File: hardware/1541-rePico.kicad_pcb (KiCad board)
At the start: 2 copper layers, 59.1 x 60 mm, 23 parts, among them IC2 VIA6522, J1 Conn_01x01_Pin, J2 RESET_1541, J3 SD Card Module Connector, J4 EXT_5V, J5 Display Power, J6 Conn_01x05_Pin, J7 Display Connector, P1 VIA_PIN_1-20, P2 VIA_PIN_21-40, SW1 RESET, U1 Pico, U2 TXS0108EPW, U3 TXS0108EPW

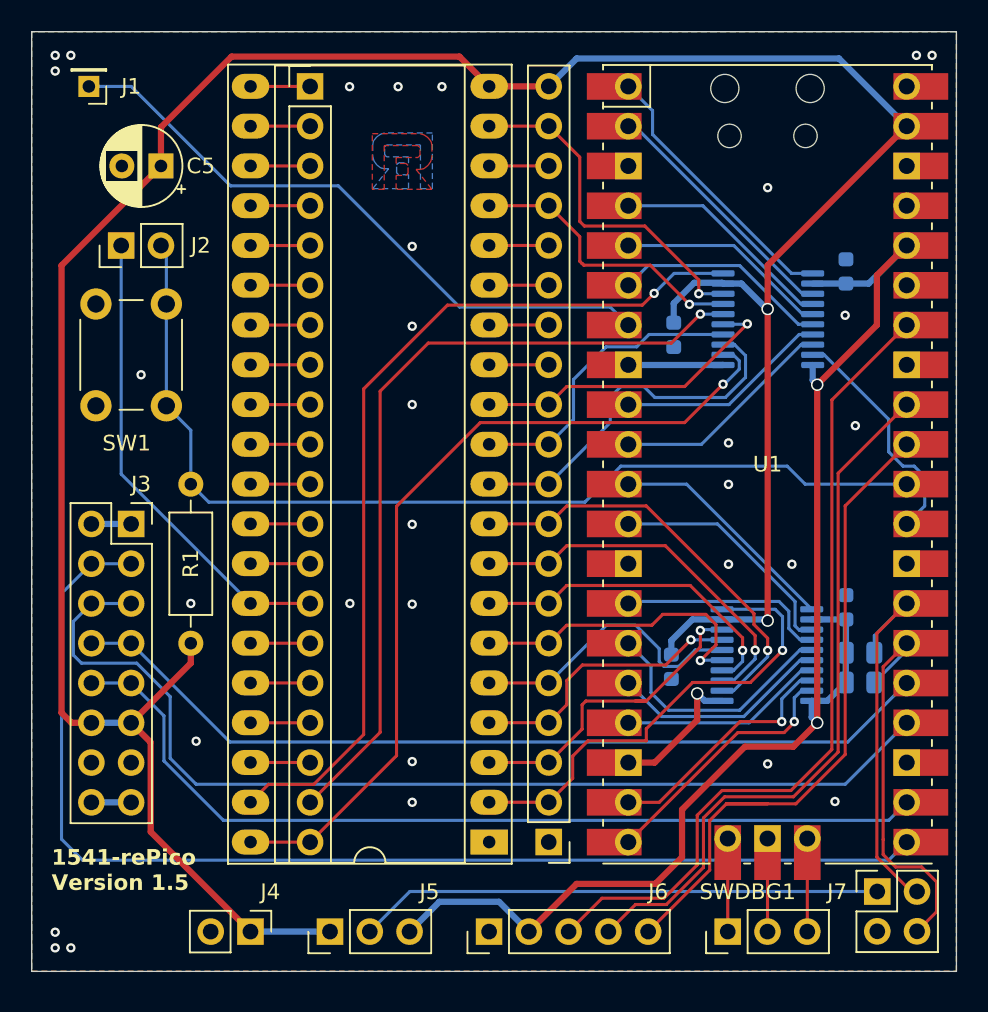
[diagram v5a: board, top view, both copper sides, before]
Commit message: PCB version 1.6
- use of SN74LVC4245A for levelshifting of PortB-Signals
-> needed an inverted Mode/OE signal for DIR (done via BSS138)
- use of BSS138 for shifting of basic signals (MTR, STP,...)
- cut off "mode/OE" pin from Gatearray -> tied to GND to not let it drive PortB
- rerouted the PCB again -> alignment of Pinheaders and vias
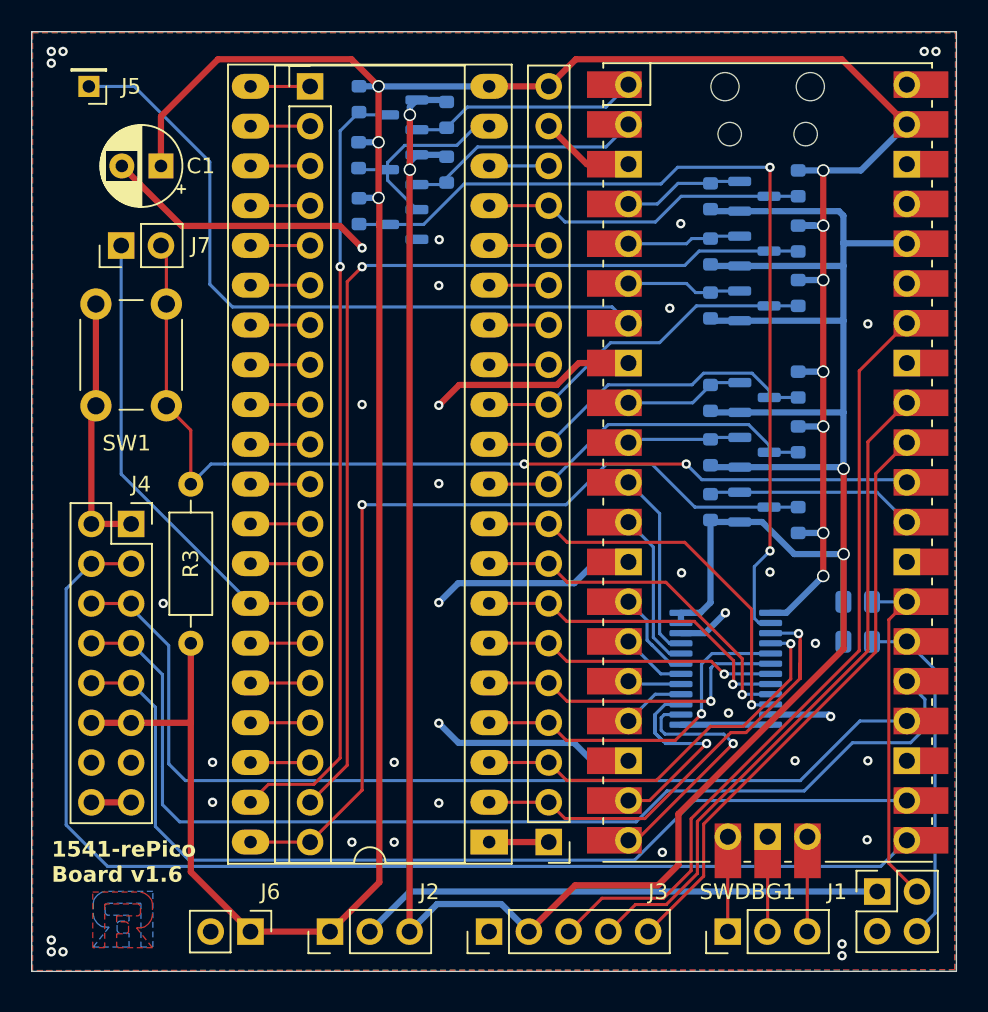
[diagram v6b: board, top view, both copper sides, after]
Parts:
- removed the C1 at (141.2, 84.4)
- removed C2, C3, C4: 0,1µF, Capacitor_SMD:C_0603_1608Metric
- removed U3: TXS0108EPW, Package_SO:TSSOP-20_4.4x6.5mm_P0.65mm
- added Q1: BSS138, Package_TO_SOT_SMD:SOT-23, B.Cu at (123.8, 77.4)
- added Q2: BSS138, Package_TO_SOT_SMD:SOT-23, B.Cu at (146.3, 91.9)
- added Q3: BSS138, Package_TO_SOT_SMD:SOT-23, B.Cu at (146.3, 88.4)
- added Q4: BSS138, Package_TO_SOT_SMD:SOT-23, B.Cu at (146.3, 82.6)
- added Q5: BSS138, Package_TO_SOT_SMD:SOT-23, B.Cu at (146.3, 75.6)
- added Q6: BSS138, Package_TO_SOT_SMD:SOT-23, B.Cu at (123.8, 73.9)
- added Q7: BSS138, Package_TO_SOT_SMD:SOT-23, B.Cu at (146.3, 95.4)
- added Q8: BSS138, Package_TO_SOT_SMD:SOT-23, B.Cu at (123.8, 70.4)
- added Q9: BSS138, Package_TO_SOT_SMD:SOT-23, B.Cu at (146.3, 79.1)
- added R10: 10k, Resistor_SMD:R_0603_1608Metric, B.Cu at (149.1, 81.7)
- added R11: 10k, Resistor_SMD:R_0603_1608Metric, B.Cu at (143.5, 75.6)
- added R12: 10k, Resistor_SMD:R_0603_1608Metric, B.Cu at (149.1, 74.7)
- added R13: 10k, Resistor_SMD:R_0603_1608Metric, B.Cu at (126.7, 73.9)
- added R14: 10k, Resistor_SMD:R_0603_1608Metric, B.Cu at (121.1, 72.9)
- added R15: 10k, Resistor_SMD:R_0603_1608Metric, B.Cu at (143.5, 95.4)
- added R16: 10k, Resistor_SMD:R_0603_1608Metric, B.Cu at (149.1, 96.2)
- added R17: 10k, Resistor_SMD:R_0603_1608Metric, B.Cu at (126.7, 70.4)
- added R18: 10k, Resistor_SMD:R_0603_1608Metric, B.Cu at (121.1, 69.4)
- added R19: 10k, Resistor_SMD:R_0603_1608Metric, B.Cu at (143.5, 79.1)
- added R20: 10k, Resistor_SMD:R_0603_1608Metric, B.Cu at (149.1, 78.3)
- added R4: 1M, Resistor_SMD:R_0603_1608Metric, B.Cu at (121.1, 76.5)
- added R5: 10k, Resistor_SMD:R_0603_1608Metric, B.Cu at (143.5, 91.9)
- added R6: 10k, Resistor_SMD:R_0603_1608Metric, B.Cu at (149.1, 91.1)
- added R7: 10k, Resistor_SMD:R_0603_1608Metric, B.Cu at (143.5, 88.4)
- added R8: 10k, Resistor_SMD:R_0603_1608Metric, B.Cu at (149.1, 87.6)
- added R9: 10k, Resistor_SMD:R_0603_1608Metric, B.Cu at (143.5, 82.5)
- U2: value TXS0108EPW -> SN74LVC4245A; footprint Package_SO:TSSOP-20_4.4x6.5mm_P0.65mm -> Package_SO:TSSOP-24_4.4x7.8mm_P0.65mm
- moved R1 3.25 mm to (152.9, 101.5)
- moved U2 2.77 mm to (144.5, 105.7)
- moved R2 2.60 mm to (152.9, 104.0)
- moved U1 0.12 mm to (147.2, 92.6)
- renumbered C5 to C1, IC2 to IC1, J7 to J1, J5 to J2, J6 to J3, J3 to J4, J1 to J5, J4 to J6, J2 to J7, R2 to R1, R3 to R2, R1 to R3
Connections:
- P1 pad 19: /VIA 6522 Sockel/MODE -> GND
- U2 pad 1: /_PA0 -> +5V
- U2 pad 10: +3.3V -> /VIA 6522 Sockel/PA7
- U2 pad 12: /VIA 6522 Sockel/PA7 -> GND
- U2 pad 13: /VIA 6522 Sockel/PA6 -> GND
- U2 pad 14: /VIA 6522 Sockel/PA5 -> /_PA7
- U2 pad 15: /VIA 6522 Sockel/PA4 -> /_PA6
- U2 pad 16: /VIA 6522 Sockel/PA3 -> /_PA5
- U2 pad 17: /VIA 6522 Sockel/PA2 -> /_PA4
- U2 pad 18: /VIA 6522 Sockel/PA1 -> /_PA3
- U2 pad 19: +5V -> /_PA2
- U2 pad 2: +3.3V -> Net-(Q1-D)
- U2 pad 20: /VIA 6522 Sockel/PA0 -> /_PA1
- U2 pad 3: /_PA1 -> /VIA 6522 Sockel/PA0
- U2 pad 4: /_PA2 -> /VIA 6522 Sockel/PA1
- U2 pad 5: /_PA3 -> /VIA 6522 Sockel/PA2
- U2 pad 6: /_PA4 -> /VIA 6522 Sockel/PA3
- U2 pad 7: /_PA5 -> /VIA 6522 Sockel/PA4
- U2 pad 8: /_PA6 -> /VIA 6522 Sockel/PA5
- U2 pad 9: /_PA7 -> /VIA 6522 Sockel/PA6
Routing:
- net +3.3V: track 86.6 -> 194.6 mm, vias 2 -> 4
- net GND: track 20.3 -> 99.2 mm, vias 32 -> 38
- net Net-(Q1-D): track 0.00 -> 58.1 mm, vias 0 -> 2
- net +5V: track 177.1 -> 193.6 mm, vias 2 -> 10
- net MOSI: track 56.2 -> 68.8 mm
- net /_PA3: track 16.1 -> 4.21 mm
- net /VIA 6522 Sockel/SOE_GA: track 52.0 -> 63.9 mm
- net /_PA4: track 14.1 -> 3.43 mm
- net /VIA 6522 Sockel/MODE: track 22.3 -> 13.1 mm, vias 1 -> 0
- net /_PA5: track 13.1 -> 4.06 mm
- net /_PA2: track 13.4 -> 5.82 mm
- net /_STP1: track 14.4 -> 7.25 mm
- net /VIA 6522 Sockel/SOE: track 57.5 -> 50.5 mm
- net /_MTR: track 13.9 -> 7.38 mm
- net /_SYNC: track 14.4 -> 8.07 mm
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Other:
- board text added: "1541-rePico Board v1.6"
- board text added: "https://github.com/fook42/1541-rePico"
- board text removed: "1541-rePico Version 1.5"
- board text removed: "https://github.com/fook42/1541-repico"

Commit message: updated PDFs for PCB v1.6
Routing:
- net GND: track 99.2 -> 99.7 mm, vias 38 -> 39
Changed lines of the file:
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@@
 	(title_block
 		(title "1541-rePico")
-		(date "2026-04-12")
+		(date "2026-04-13")
 		(rev "1.6")
 	)
@@
 	)
 	(segment
-		(start 135.6276 73.5196)
+		(start 126.2026 74.58313)
+		(end 128.41613 72.3696)
+		(width 0.4)
+		(layer "F.Cu")
+		(net 2)
+	)
+	(segment
+		(start 131.4576 71.0896)
 		(end 133.1976 71.0896)
 		(width 0.4)
@@
 	)
 	(segment
+		(start 131.3776 72.3696)
+		(end 131.3776 71.1696)
+		(width 0.4)
+		(layer "F.Cu")
+		(net 2)
+	)
+	(segment
 		(start 103.9876 89.2396)
 		(end 104.2776 88.9496)
@@
 	)
 	(segment
+		(start 131.3776 71.1696)
+		(end 131.4576 71.0896)
+		(width 0.4)
+		(layer "F.Cu")
+		(net 2)
+	)
+	(segment
 		(start 106.5276 114.2746)
 		(end 103.9876 114.2746)
@@
 	)
 	(segment
-		(start 103.9876 96.4946)
-		(end 103.9876 89.2396)
+		(start 134.7976 71.0896)
+		(end 133.1976 71.0896)
 		(width 0.4)
 		(layer "F.Cu")
@@
 	)
 	(segment
-		(start 105.9326 73.6346)
-		(end 109.7616 77.4636)
+		(start 106.5276 96.4946)
+		(end 103.9876 96.4946)
 		(width 0.4)
 		(layer "F.Cu")
@@
 	)
 	(segment
-		(start 133.1976 116.8096)
-		(end 129.3926 116.8096)
+		(start 134.8276 73.5196)
+		(end 134.8276 71.1196)
+		(width 0.4)
+		(layer "F.Cu")
+		(net 2)
+	)
+	(segment
+		(start 134.8276 71.1196)
+		(end 134.7976 71.0896)
+		(width 0.4)
+		(layer "F.Cu")
+		(net 2)
+	)
+	(segment
+		(start 128.41613 72.3696)
+		(end 131.3776 72.3696)
+		(width 0.4)
+		(layer "F.Cu")
+		(net 2)
+	)
+	(segment
+		(start 105.9326 73.6346)
+		(end 109.7616 77.4636)
 		(width 0.4)
 		(layer "F.Cu")
@@
 	)
 	(segment
-		(start 104.2776 88.9496)
-		(end 104.2776 82.4496)
+		(start 133.1976 116.8096)
+		(end 129.3926 116.8096)
 		(width 0.4)
 		(layer "F.Cu")
@@
 	)
 	(segment
-		(start 103.9876 96.4946)
-		(end 106.5276 96.4946)
+		(start 138.2876 73.5196)
+		(end 134.8276 73.5196)
 		(width 0.4)
 		(layer "F.Cu")
@@
 	)
 	(segment
-		(start 138.2876 73.5196)
-		(end 135.6276 73.5196)
+		(start 126.2026 78.3446)
+		(end 126.2026 74.58313)
 		(width 0.4)
 		(layer "F.Cu")
@@
 	)
 	(via
+		(at 111.7276 116.8196)
+		(size 0.6)
+		(drill 0.3)
+		(layers "F.Cu" "B.Cu")
+		(free yes)
+		(net 2)
+	)
+	(via
 		(at 141.6776 99.6196)
 		(size 0.6)
@@
 	)
 	(via
-		(at 108.5776 101.5696)
+		(at 110.3276 101.5696)
 		(size 0.6)
 		(drill 0.3)
